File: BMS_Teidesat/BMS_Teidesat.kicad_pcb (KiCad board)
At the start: 2 copper layers, 90.2 x 95.9 mm, 50 parts, among them J1 Battery, J2 Battery, U1 AD8605ACBZ-REEL7, U2 AD8606ARMZ-REEL, U3 ADA4940-1ACPZ-R7, U4 ACS37002LMCATR-050B5, U5 AD7091R-8BCPZ-RL7, U6 CSD86311W1723, U7 AD8605ACBZ-REEL7, U8 STM32G474VET6, U9 TMS5703137DPGEQQ1

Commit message: Ajustes PCB
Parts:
- removed the U8 at (45.0, 77.0)
- added C3: 10n, Capacitor_SMD:C_0805_2012Metric, F.Cu at (30.4, 172.3)
- added C4: 10n, Capacitor_SMD:C_0805_2012Metric, F.Cu at (30.4, 175.3)
- added C5: 10n, Capacitor_SMD:C_0805_2012Metric, F.Cu at (30.4, 178.4)
- added C6: 10n, Capacitor_SMD:C_0805_2012Metric, F.Cu at (30.4, 181.4)
- added C7: 10n, Capacitor_SMD:C_0805_2012Metric, F.Cu at (30.4, 184.4)
- added C8: 10n, Capacitor_SMD:C_0805_2012Metric, F.Cu at (30.4, 187.4)
- added D3: SS14, Huellas BMS:DIOM8059X256N, F.Cu at (22.8, 165.0)
- added D4: SS14, Huellas BMS:DIOM8059X256N, F.Cu at (22.8, 172.4)
- added D5: SS14, Huellas BMS:DIOM8059X256N, F.Cu at (22.8, 179.9)
- added D6: SS14, Huellas BMS:DIOM8059X256N, F.Cu at (22.8, 187.3)
- added R10: 10, Resistor_SMD:R_0201_0603Metric, F.Cu at (33.8, 188.3)
- added R21: 10, Resistor_SMD:R_0201_0603Metric, F.Cu at (33.8, 190.1)
- added R22: 10, Resistor_SMD:R_0201_0603Metric, F.Cu at (36.3, 184.8)
- added R23: 10, Resistor_SMD:R_0201_0603Metric, F.Cu at (36.3, 186.6)
- added R25: 10, Resistor_SMD:R_0201_0603Metric, F.Cu at (36.3, 188.3)
- added R26: 10, Resistor_SMD:R_0201_0603Metric, F.Cu at (36.3, 190.1)
- added R27: 10, Resistor_SMD:R_0201_0603Metric, F.Cu at (38.7, 184.8)
- added R28: 10, Resistor_SMD:R_0201_0603Metric, F.Cu at (38.7, 186.6)
- added R29: 10, Resistor_SMD:R_0201_0603Metric, F.Cu at (38.7, 188.3)
- added R30: 10, Resistor_SMD:R_0201_0603Metric, F.Cu at (38.7, 190.1)
- added R8: 10, Resistor_SMD:R_0201_0603Metric, F.Cu at (33.8, 184.8)
- added R9: 10, Resistor_SMD:R_0201_0603Metric, F.Cu at (33.8, 186.6)
- added U1: MCP1407-E_SN, Huellas BMS:SOIC127P600X175-8N, F.Cu at (36.9, 174.1)
- added U10: IPT004N03L, Huellas BMS:PG-HSOF-8-1, F.Cu at (52.0, 144.1)
- added U11: IPT004N03L, Huellas BMS:PG-HSOF-8-1, F.Cu at (63.4, 144.1)
- added U12: IPT004N03L, Huellas BMS:PG-HSOF-8-1, F.Cu at (74.8, 144.1)
- added U13: MCP1407-E_SN, Huellas BMS:SOIC127P600X175-8N, F.Cu at (36.9, 180.7)
- added U4: IPT004N03L, Huellas BMS:PG-HSOF-8-1, F.Cu at (17.8, 144.1)
- added U5: IPT004N03L, Huellas BMS:PG-HSOF-8-1, F.Cu at (29.2, 144.1)
- added U6: IPT004N03L, Huellas BMS:PG-HSOF-8-1, F.Cu at (40.6, 144.1)
- moved U9 131.5 mm to (40.4, 158.6)
- moved D1 116.9 mm to (22.8, 150.1), turned to 0 degrees
- moved D2 107.9 mm to (22.8, 157.5), turned to 0 degrees
- moved Termistor1 76.9 mm to (57.3, 148.5)
- renumbered C5 to C10, C6 to C11, C7 to C12, C8 to C13, R10 to R11, R11 to R12, R9 to R13, R12 to R14, R13 to R15, R14 to R16, R15 to R17, R16 to R18, R17 to R19, R18 to R20, R19 to R24, R5 to R31, R6 to R5, R7 to R6, R8 to R7, U5 to U14, U7 to U15, U1 to U3, U3 to U7, U4 to U8
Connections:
- D1 pad 1: /+BATTERY -> /BATTERY
- D1 pad 2: Net-(D1-A) -> /MOSFET1
- D2 pad 1: /+BATTERY -> /BATTERY
- D2 pad 2: /EPS -> /MOSFET2
- H1 pad 47: unconnected-(H1-Pin_47-Pad47) -> +3V3
- H1 pad 48: unconnected-(H1-Pin_48-Pad48) -> +3V3
- H1 pad 49: unconnected-(H1-Pin_49-Pad49) -> +3V3
- H1 pad 50: unconnected-(H1-Pin_50-Pad50) -> +3V3
- H1 pad 51: unconnected-(H1-Pin_51-Pad51) -> +3V3
- H1 pad 52: unconnected-(H1-Pin_52-Pad52) -> +3V3
- H2 pad 18: unconnected-(H2-Pin_18-Pad18) -> +3V3
- H2 pad 19: unconnected-(H2-Pin_19-Pad19) -> +3V3
- H2 pad 20: unconnected-(H2-Pin_20-Pad20) -> +3V3
- H2 pad 21: GND -> unconnected-(H2-Pin_21-Pad21)
- H2 pad 22: GND -> unconnected-(H2-Pin_22-Pad22)
- H2 pad 25: +5V -> unconnected-(H2-Pin_25-Pad25)
- H2 pad 26: +5V -> unconnected-(H2-Pin_26-Pad26)
- H2 pad 27: +3V3 -> unconnected-(H2-Pin_27-Pad27)
- H2 pad 28: +3V3 -> unconnected-(H2-Pin_28-Pad28)
- H2 pad 29: GND -> unconnected-(H2-Pin_29-Pad29)
- H2 pad 30: GND -> unconnected-(H2-Pin_30-Pad30)
- H2 pad 31: GND -> unconnected-(H2-Pin_31-Pad31)
- H2 pad 32: GND -> unconnected-(H2-Pin_32-Pad32)
- H2 pad 45: +BATT -> unconnected-(H2-Pin_45-Pad45)
- H2 pad 46: +BATT -> unconnected-(H2-Pin_46-Pad46)
- J1 pad 1: Net-(J1-Pin_1) -> /BATTERY
- R1 pad 1: Net-(J1-Pin_1) -> /BATTERY
- U8 pad 1: /+BATTERY -> /CURRENT S
- U8 pad 2: /+BATTERY -> /CURRENT S
- U8 pad 3: /+BATTERY -> /CURRENT S
- U8 pad 4: /+BATTERY -> /CURRENT S
- U8 pad 5: /+LOAD -> /MOSFET3
- U8 pad 6: /+LOAD -> /MOSFET3
- U8 pad 7: /+LOAD -> /MOSFET3
- U8 pad 8: /+LOAD -> /MOSFET3
- U9 pad 105: unconnected-(U9-MIBSPI1NCS[0]-Pad105) -> /CS
- U9 pad 14: unconnected-(U9-GIOA[5]-Pad14) -> /RESET
- U9 pad 16: unconnected-(U9-GIOA[6]-Pad16) -> /CONTROL1
- U9 pad 22: unconnected-(U9-GIOA[7]-Pad22) -> /CONTROL2
- U9 pad 9: unconnected-(U9-GIOA[2]-Pad9) -> /GIOA
- U9 pad 93: unconnected-(U9-MIBSPI1SIMO-Pad93) -> /MOSI MC
- U9 pad 94: unconnected-(U9-MIBSPI1SOMI-Pad94) -> /OUT CAD
- U9 pad 95: unconnected-(U9-MIBSPI1CLK-Pad95) -> /CLOCK MC
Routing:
- net Net-(J1-Pin_1): track 3.88 -> 0.00 mm
- net /BATTERY: track 0.00 -> 3.88 mm

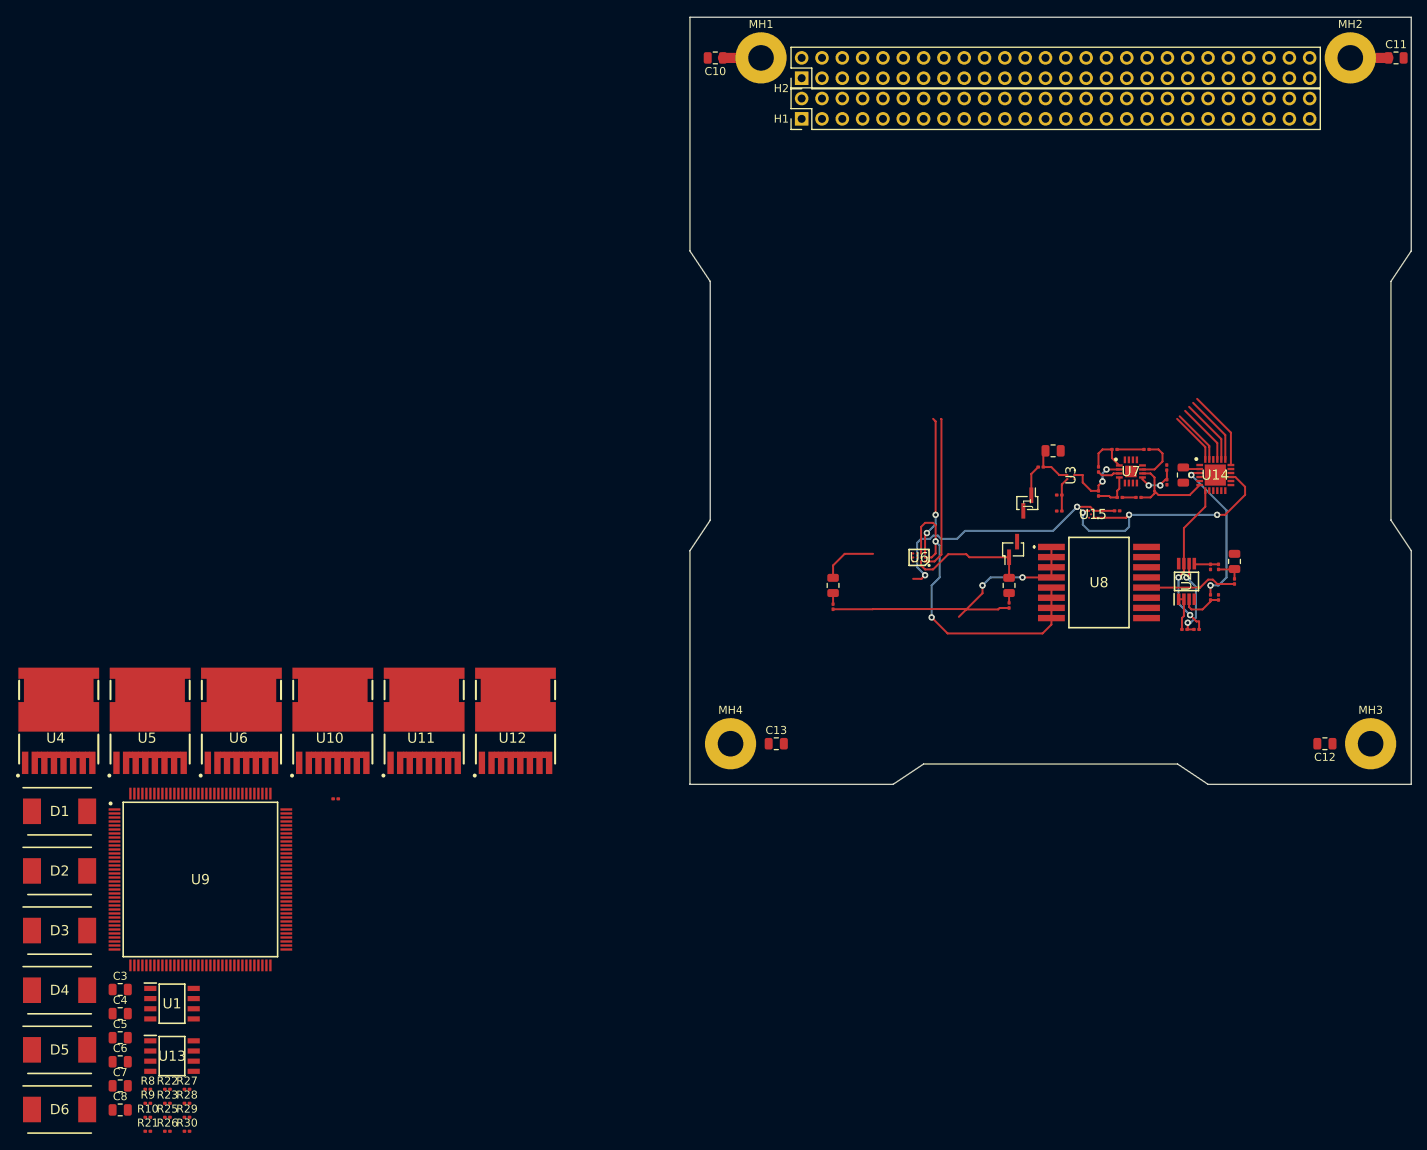
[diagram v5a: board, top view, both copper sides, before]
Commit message: Circuito de potencia PCB
Se ha elaborado el circuito de potencia de en la PCB incorporando los 3 mosfets y los 3 sensores de temperatura.

Co-Authored-By: Angel-Castro-Vega <236372966+Angel-Castro-Vega@users.noreply.github.com>
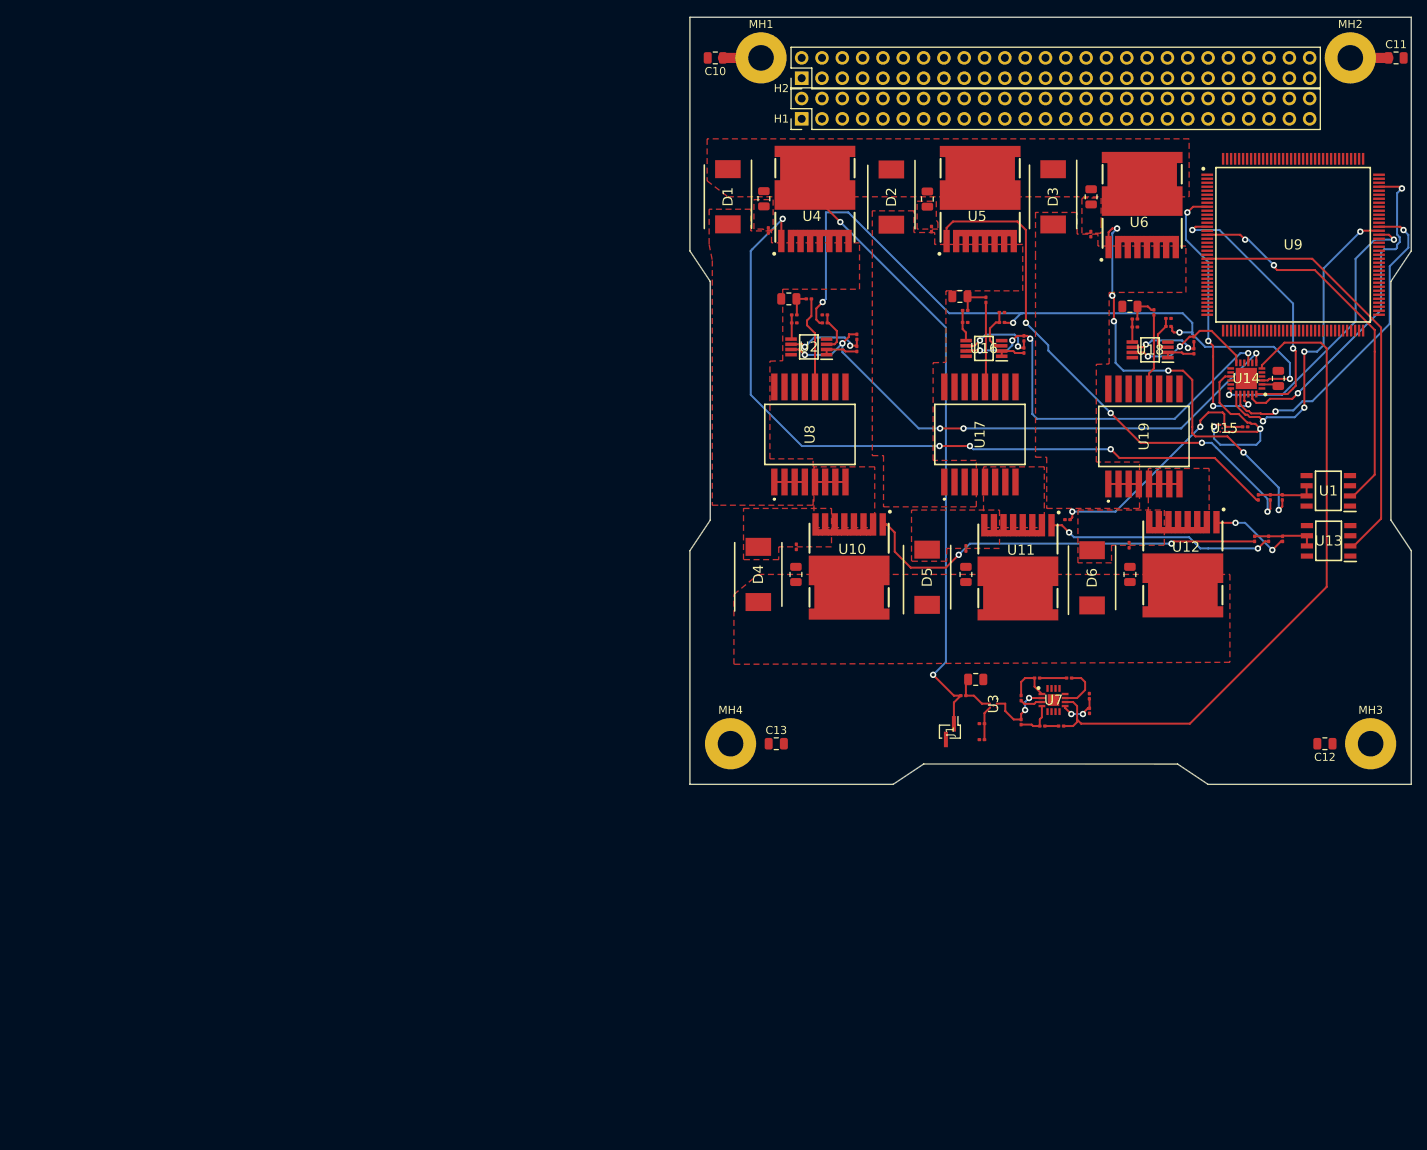
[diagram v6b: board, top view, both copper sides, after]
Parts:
- removed the C3 at (141.5, 121.8)
- removed the C4 at (119.5, 121.8)
- removed J2: Battery, Connector_PinSocket_1.00mm:PinSocket_1x02_P1.00mm_Vertical_SMD_Pin1Left
- removed the R20 at (141.5, 124.3)
- removed the R21 at (119.5, 124.5)
- removed the U6 at (130.2, 118.3)
- added C14: 1n, Capacitor_SMD:C_0805_2012Metric, F.Cu at (135.3, 85.7)
- added C15: 1n, Capacitor_SMD:C_0805_2012Metric, F.Cu at (156.6, 87.0)
- added R32: 50,5K, Resistor_SMD:R_0201_0603Metric, F.Cu at (143.3, 91.0)
- added R33: 50,5k, Resistor_SMD:R_0201_0603Metric, F.Cu at (136.0, 89.0)
- added R34: 80,6K, Resistor_SMD:R_0201_0603Metric, F.Cu at (143.3, 92.5)
- added R35: 80,6K, Resistor_SMD:R_0201_0603Metric, F.Cu at (136.0, 87.5)
- added R36: 40,2K, Resistor_SMD:R_0201_0603Metric, F.Cu at (140.6, 89.0)
- added R37: 10K, Resistor_SMD:R_0201_0603Metric, F.Cu at (140.6, 87.7)
- added R38: 100, Resistor_SMD:R_0201_0603Metric, F.Cu at (138.6, 86.1)
- added R39: 50,5K, Resistor_SMD:R_0201_0603Metric, F.Cu at (164.6, 91.0)
- added R40: 50,5k, Resistor_SMD:R_0201_0603Metric, F.Cu at (157.2, 89.5)
- added R41: 80,6K, Resistor_SMD:R_0201_0603Metric, F.Cu at (164.6, 92.5)
- added R42: 80,6K, Resistor_SMD:R_0201_0603Metric, F.Cu at (157.2, 88.5)
- added R43: 40,2K, Resistor_SMD:R_0201_0603Metric, F.Cu at (161.4, 89.5)
- added R44: 10K, Resistor_SMD:R_0201_0603Metric, F.Cu at (161.4, 88.5)
- added R45: 100, Resistor_SMD:R_0201_0603Metric, F.Cu at (159.6, 87.7)
- added U16: AD8606ARMZ-REEL, Huellas BMS:SOP65P490X110-8N, F.Cu at (138.3, 92.2)
- added U17: ACS37002LMCATR-050B5, Huellas BMS:ACS37002LMCA050U5, F.Cu at (137.8, 103.0)
- added U18: AD8606ARMZ-REEL, Huellas BMS:SOP65P490X110-8N, F.Cu at (159.1, 92.4)
- added U19: ACS37002LMCATR-050B5, Huellas BMS:ACS37002LMCA050U5, F.Cu at (158.3, 103.2)
- moved R10 161.6 mm to (175.7, 110.8), turned to -90 degrees
- moved R9 159.4 mm to (174.2, 110.8), turned to -90 degrees
- moved C4 158.6 mm to (151.8, 73.2), turned to -90 degrees
- moved U13 158.3 mm to (181.4, 116.2), turned to 180 degrees
- moved U1 158.1 mm to (181.4, 110.0), turned to 180 degrees
- moved U9 158.0 mm to (177.0, 79.2)
- moved R22 157.3 mm to (151.7, 77.9), turned to -90 degrees
- moved R8 157.3 mm to (172.7, 110.8), turned to -90 degrees
- moved R30 155.7 mm to (175.7, 116.0), turned to -90 degrees
- moved D3 154.4 mm to (147.0, 73.2), turned to -90 degrees
- moved R29 153.3 mm to (173.9, 116.0), turned to -90 degrees
- moved R28 151.0 mm to (172.2, 116.0), turned to -90 degrees
- moved R21 149.4 mm to (131.8, 77.3), turned to -90 degrees
- moved D6 145.2 mm to (151.9, 120.9), turned to 90 degrees
- moved C8 142.9 mm to (156.6, 120.5), turned to 90 degrees
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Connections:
- net /+HALL renamed /+HALL1
- D1 pad 2: /MOSFET1 -> /CURRENT_1
- D2 pad 2: /MOSFET2 -> /CURRENT_2
- D3 pad 2: /CURRENT S -> /CURRENT_3
- R21 pad 2: /MOSFET2 -> /CURRENT_2
- R22 pad 2: /CURRENT S -> /CURRENT_3
- R23 pad 2: /MOSFET1 -> /CURRENT_1
- U14 pad 12: unconnected-(U14-VIN5-Pad12) -> /+HALL3
- U14 pad 9: unconnected-(U14-VIN4-Pad9) -> /+HALL2
- U4 pad 2: /MOSFET1 -> /CURRENT_1
- U4 pad 3: /MOSFET1 -> /CURRENT_1
- U4 pad 4: /MOSFET1 -> /CURRENT_1
- U4 pad 5: /MOSFET1 -> /CURRENT_1
- U4 pad 6: /MOSFET1 -> /CURRENT_1
- U4 pad 7: /MOSFET1 -> /CURRENT_1
- U4 pad 8: /MOSFET1 -> /CURRENT_1
- U5 pad 2: /MOSFET2 -> /CURRENT_2
- U5 pad 3: /MOSFET2 -> /CURRENT_2
- U5 pad 4: /MOSFET2 -> /CURRENT_2
- U5 pad 5: /MOSFET2 -> /CURRENT_2
- U5 pad 6: /MOSFET2 -> /CURRENT_2
- U5 pad 7: /MOSFET2 -> /CURRENT_2
- U5 pad 8: /MOSFET2 -> /CURRENT_2
- U6 pad 2: /CURRENT S -> /CURRENT_3
- U6 pad 3: /CURRENT S -> /CURRENT_3
- U6 pad 4: /CURRENT S -> /CURRENT_3
- U6 pad 5: /CURRENT S -> /CURRENT_3
- U6 pad 6: /CURRENT S -> /CURRENT_3
- U6 pad 7: /CURRENT S -> /CURRENT_3
- U6 pad 8: /CURRENT S -> /CURRENT_3
- U8 pad 1: /CURRENT S -> /CURRENT_1
- U8 pad 2: /CURRENT S -> /CURRENT_1
- U8 pad 3: /CURRENT S -> /CURRENT_1
- U8 pad 4: /CURRENT S -> /CURRENT_1
- U8 pad 5: /MOSFET3 -> /MOSFET1
- U8 pad 6: /MOSFET3 -> /MOSFET1
- U8 pad 7: /MOSFET3 -> /MOSFET1
- U8 pad 8: /MOSFET3 -> /MOSFET1
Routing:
- net Net-(U4-G): track 0.00 -> 95.4 mm, vias 0 -> 4
- net /BATTERY: track 3.88 -> 91.1 mm, vias 0 -> 2
- net /REFOUT: track 19.4 -> 93.1 mm, vias 2 -> 4
- net /+VBAT: track 12.0 -> 83.9 mm
- net Net-(U5-G): track 0.00 -> 67.1 mm, vias 0 -> 4
- net Net-(U6-G): track 0.00 -> 55.4 mm, vias 0 -> 6
- net /+HALL1: track 20.0 -> 71.6 mm, vias 2 -> 5
- net Net-(U10-G): track 0.00 -> 51.5 mm, vias 0 -> 2
- net /+HALL2: track 0.00 -> 50.7 mm, vias 0 -> 4
- net /+LOAD: track 41.5 -> 0.00 mm, vias 2 -> 0
- net /+BATTERY: track 40.1 -> 0.00 mm, vias 2 -> 0
- net /CONTROL2: track 17.5 -> 54.4 mm, vias 2 -> 0
- net /CS: track 6.93 -> 42.0 mm, vias 0 -> 2
- net /CLOCK MC: track 8.24 -> 41.3 mm, vias 0 -> 2
- net /OUT CAD: track 8.74 -> 39.7 mm, vias 0 -> 4
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- added copper zone on F.Cu, net /BATTERY
- added copper zone on F.Cu, net /CURRENT_1
- added copper zone on F.Cu, net /CURRENT_2
- added copper zone on F.Cu, net /CURRENT_3
- added copper zone on F.Cu, net /MOSFET1
- added copper zone on F.Cu, net /MOSFET2
- added copper zone on F.Cu, net /MOSFET3
- added copper zone on F.Cu, net /OUT EPS
- added copper zone on F.Cu, net Net-(C3-Pad2)
- added copper zone on F.Cu, net Net-(C4-Pad2)
- added copper zone on F.Cu, net Net-(C5-Pad2)
